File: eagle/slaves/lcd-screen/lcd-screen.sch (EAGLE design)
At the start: 23 parts, among them CON1 SPI, IC1 MCP1703CB, J1 RJ12RIGHTANGLE-I2C, J2 RJ12RIGHTANGLE-I2C, J3 RJ12RIGHTANGLE-I2C, U1 ATMEGA328P_TQFP

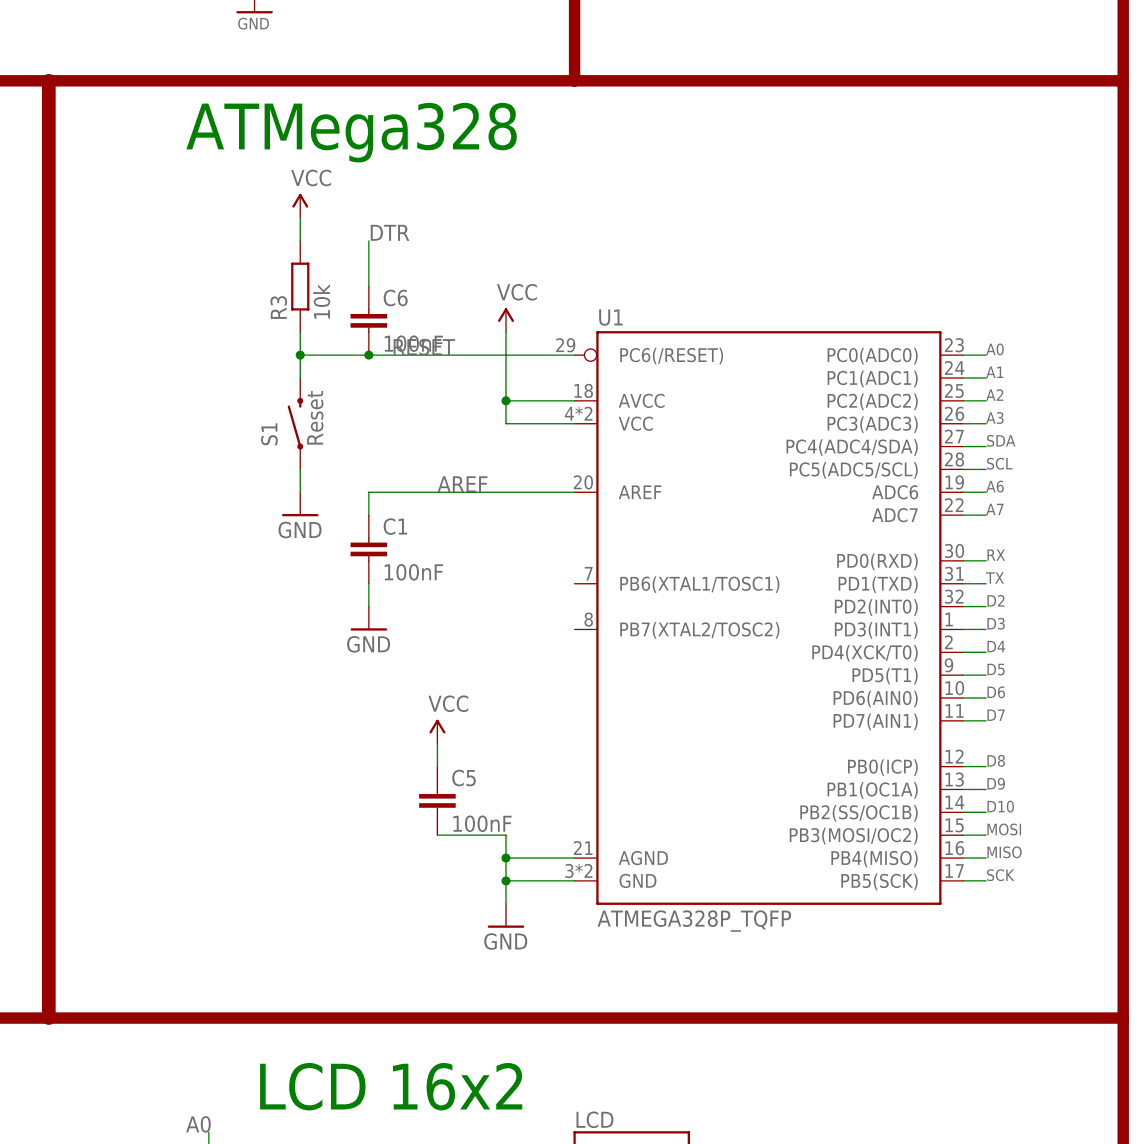
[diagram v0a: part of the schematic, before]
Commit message: rename lcd-slave and add address selector
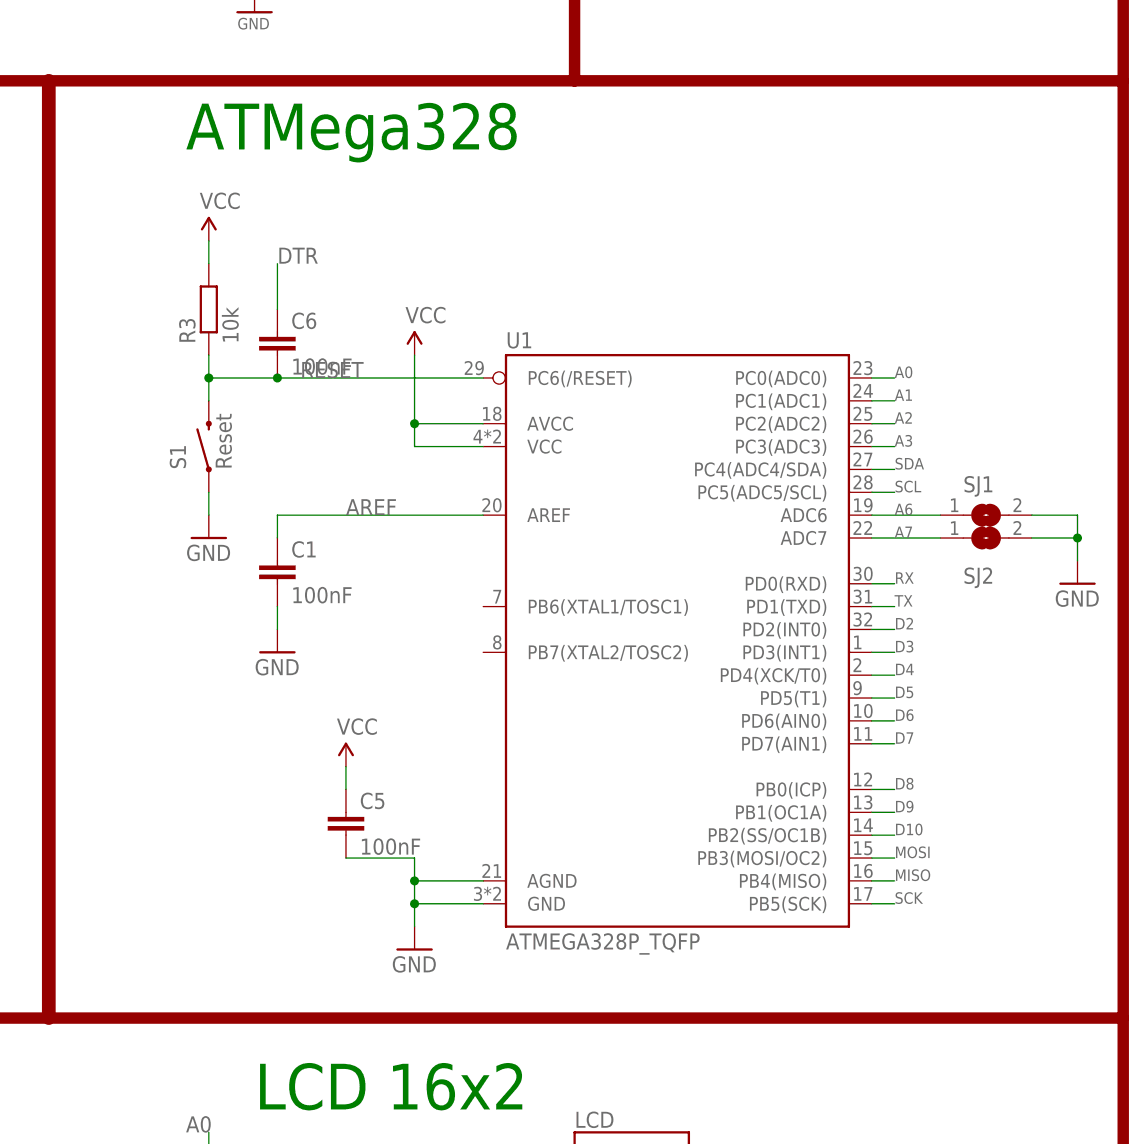
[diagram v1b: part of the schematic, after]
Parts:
- added SJ1, SJ2: (no value), jumper:SJ
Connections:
- net A6: now also SJ1.1
- net A7: now also SJ2.1
- net GND: now also SJ1.2, SJ2.2
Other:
- moved on the sheet: C1, C5, C6, R3, S1, U1
